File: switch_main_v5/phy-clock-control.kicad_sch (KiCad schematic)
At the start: 36 parts, among them Q1101 DMN21D2UFB-7B, Q1102 DMN21D2UFB-7B, Q1103 DMN21D2UFB-7B, U1101 NX3L4051HRZ, U1102 LMK1C1104DQFR, U1103 LMK1C1104DQFR

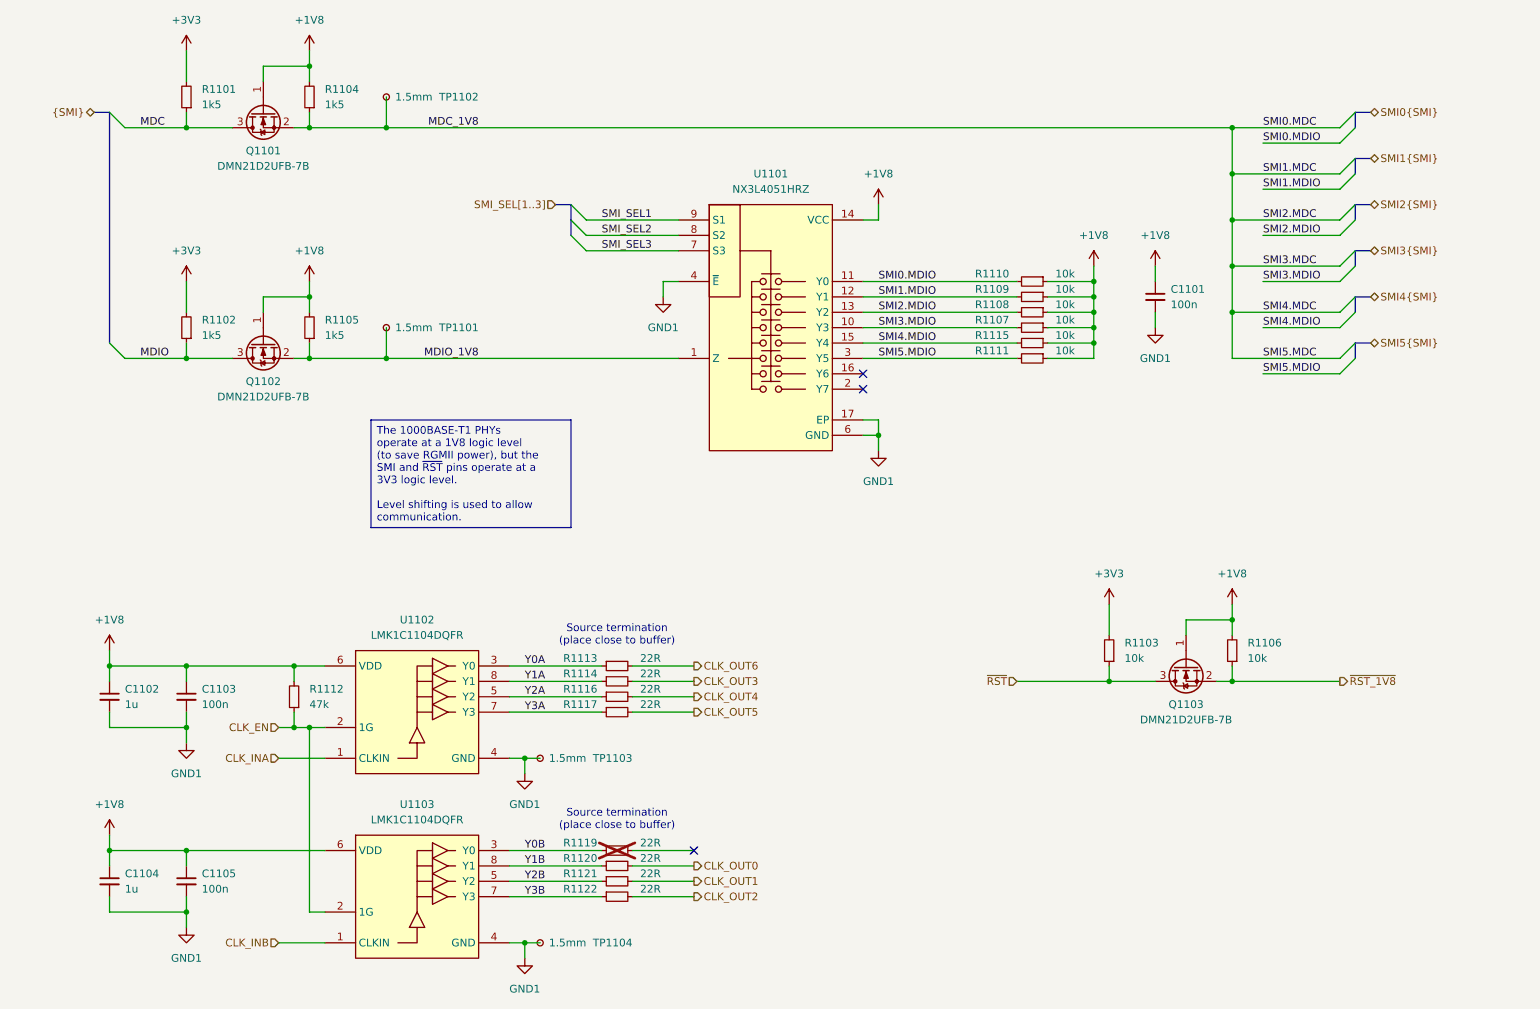
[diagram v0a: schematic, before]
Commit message: Updated 1v0_buck_converter feedback resistors
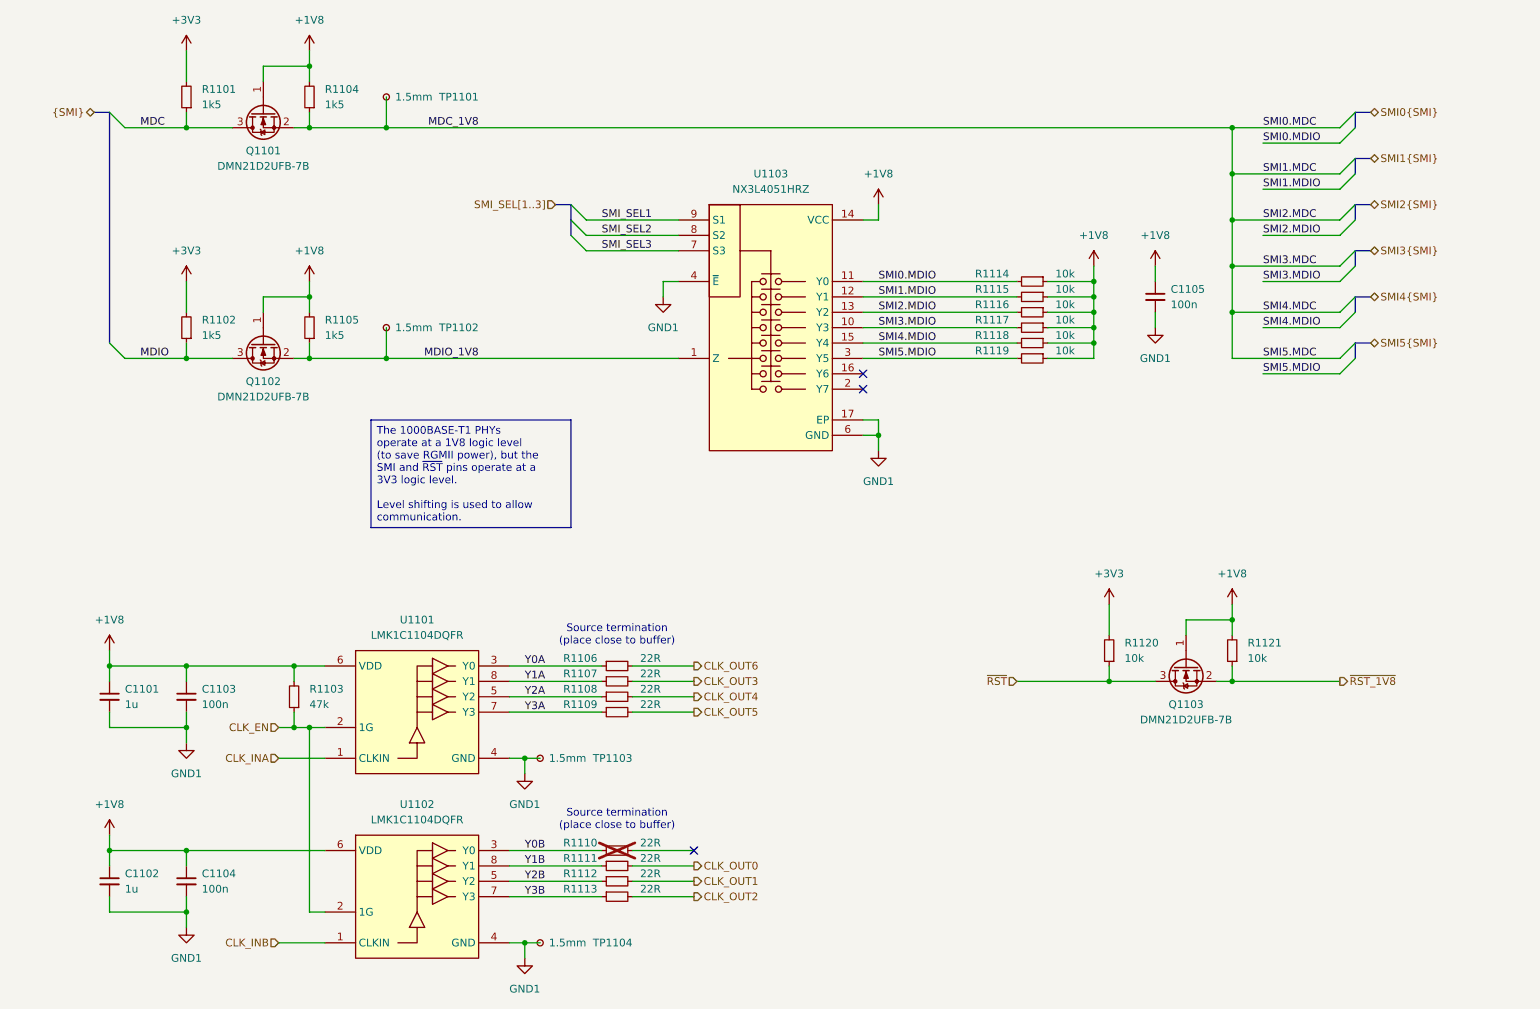
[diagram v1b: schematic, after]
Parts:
- renumbered C1102 to C1101, C1104 to C1102, C1105 to C1104, C1101 to C1105, R1112 to R1103, R1113 to R1106, R1114 to R1107, R1116 to R1108, R1117 to R1109, R1119 to R1110, R1120 to R1111, R1121 to R1112, R1122 to R1113, R1110 to R1114, R1109 to R1115, R1108 to R1116, R1107 to R1117, R1115 to R1118, R1111 to R1119, R1103 to R1120, R1106 to R1121, TP1102 to TP1101, TP1101 to TP1102, U1102 to U1101, U1103 to U1102, U1101 to U1103

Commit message: Changed main 3V3 regulator to 3A, added switch 2 crystal & other changes
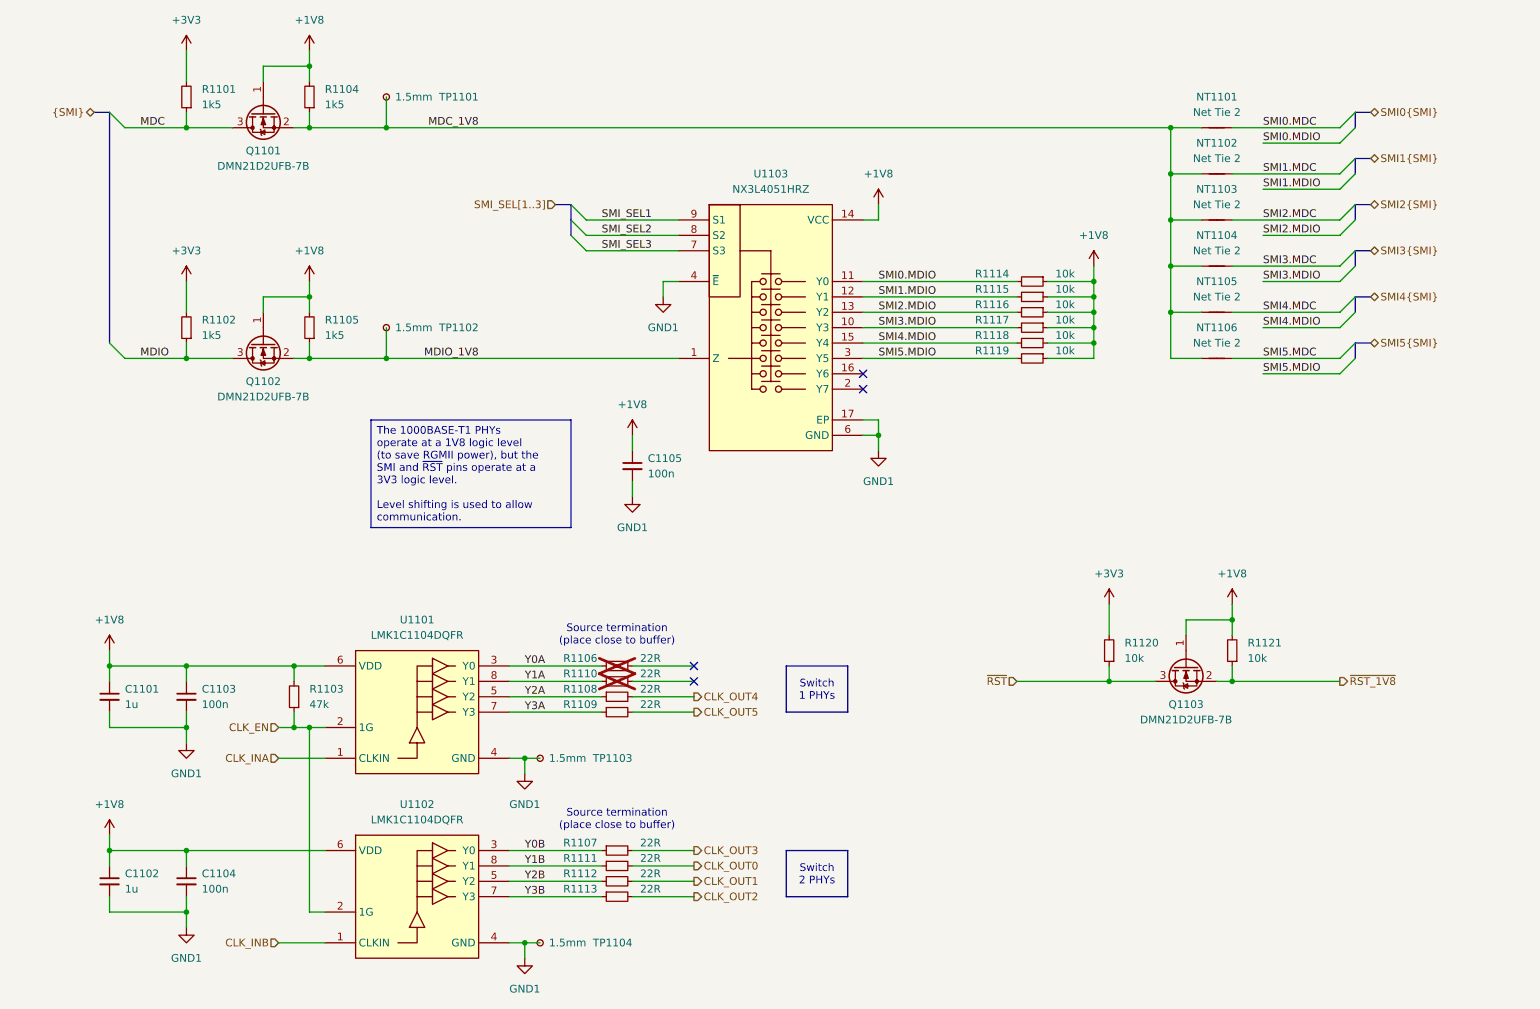
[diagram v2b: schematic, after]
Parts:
- added NT1101, NT1102, NT1103, NT1104, NT1105, NT1106: Net Tie 2, project_footprints:NetTie-2_SMD_Pad0.15mm, symbol NET-TIE:NetTie_2
- R1106: now not fitted; now left out of the parts list
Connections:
- net MDC_1V8: now also NT1101.1, NT1102.1, NT1103.1, NT1104.1, NT1105.1, NT1106.1
- net Y0B: now also R1107.1; no longer R1110.1
- net Y1A: now also R1110.1; no longer R1107.1
- net CLK_OUT6: no longer names the net of R1106.2
- new net SMI0.MDC: NT1101.2
- new net SMI1.MDC: NT1102.2
- new net SMI2.MDC: NT1103.2
- new net SMI3.MDC: NT1104.2
- new net SMI4.MDC: NT1105.2
- new net SMI5.MDC: NT1106.2
- no-connect marks 3 -> 4
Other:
- moved on the sheet: C1105, R1107, R1110

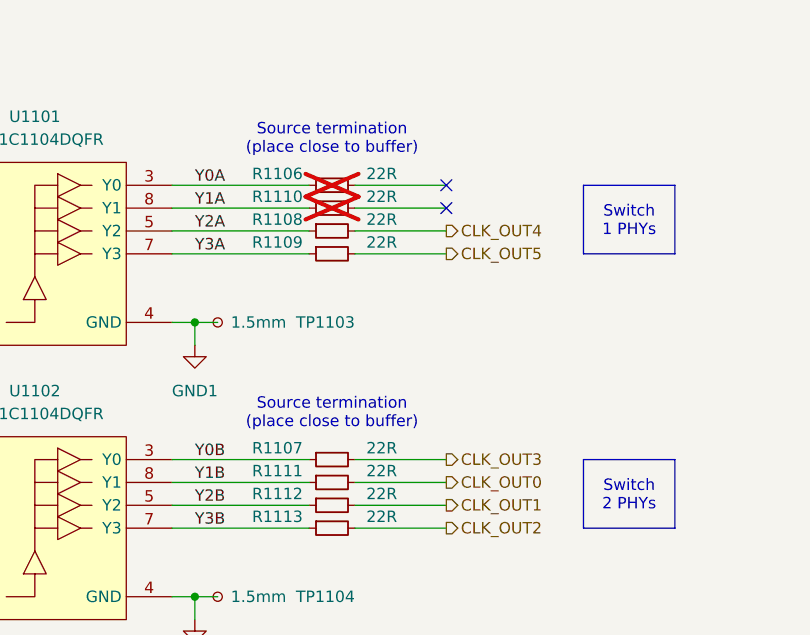
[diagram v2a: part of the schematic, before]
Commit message: Routed switch 1 clocking
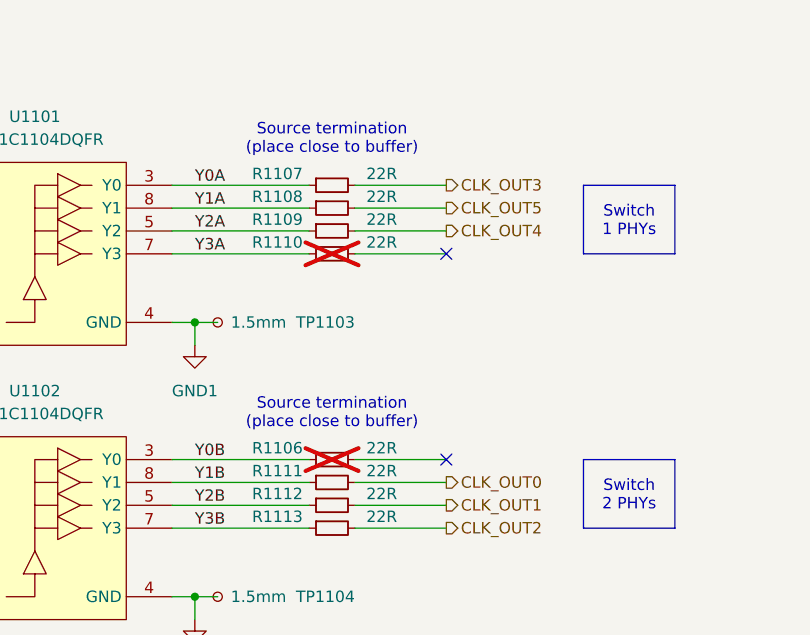
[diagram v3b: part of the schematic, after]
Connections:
- net CLK_OUT4: now also R1109.2; no longer R1108.2
- net CLK_OUT5: now also R1108.2; no longer R1109.2
- net Y0A: now also R1107.1; no longer R1106.1
- net Y0B: now also R1106.1; no longer R1107.1
- net Y1A: now also R1108.1; no longer R1110.1
- net Y2A: now also R1109.1; no longer R1108.1
- net Y3A: now also R1110.1; no longer R1109.1
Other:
- moved on the sheet: R1106, R1107, R1108, R1109, R1110
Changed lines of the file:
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@@
 	)
 	(no_connect
-		(at 139.7 132.08)
+		(at 139.7 137.16)
 	)
 	(no_connect
@@
 	)
 	(no_connect
-		(at 139.7 129.54)
+		(at 139.7 160.02)
 	)
 	(no_connect
@@
 	(hierarchical_label "CLK_OUT3"
 		(shape output)
-		(at 139.7 160.02 0)
+		(at 139.7 129.54 0)
 		(effects
 			(font
@@
 	(hierarchical_label "CLK_OUT5"
 		(shape output)
-		(at 139.7 137.16 0)
+		(at 139.7 132.08 0)
 		(effects
 			(font
@@
 	(symbol
 		(lib_id "Device:R_Small")
-		(at 127 160.02 90)
+		(at 127 129.54 90)
 		(mirror x)
 		(unit 1)
@@
 		(dnp no)
 		(property "Reference" "R1107"
-			(at 118.11 158.75 90)
+			(at 118.11 128.27 90)
 			(effects
 				(font
@@
 		)
 		(property "Value" "22R"
-			(at 130.81 158.75 90)
+			(at 130.81 128.27 90)
 			(effects
 				(font
@@
 		)
 		(property "Footprint" "Resistor_SMD:R_0402_1005Metric"
-			(at 127 160.02 0)
+			(at 127 129.54 0)
 			(effects
 				(font
@@
 		)
 		(property "Datasheet" "~"
-			(at 127 160.02 0)
+			(at 127 129.54 0)
 			(effects
 				(font
@@
 		)
 		(property "Description" "Resistor, small symbol"
-			(at 127 160.02 0)
+			(at 127 129.54 0)
 			(effects
 				(font
@@
 	(symbol
 		(lib_id "Device:R_Small")
-		(at 127 132.08 90)
+		(at 127 137.16 90)
 		(mirror x)
 		(unit 1)
@@
 		(dnp yes)
 		(property "Reference" "R1110"
-			(at 118.11 130.81 90)
+			(at 118.11 135.89 90)
 			(effects
 				(font
@@
 		)
 		(property "Value" "22R"
-			(at 130.81 130.81 90)
+			(at 130.81 135.89 90)
 			(effects
 				(font
@@
 		)
 		(property "Footprint" "Resistor_SMD:R_0402_1005Metric"
-			(at 127 132.08 0)
+			(at 127 137.16 0)
 			(effects
 				(font
@@
 		)
 		(property "Datasheet" "~"
-			(at 127 132.08 0)
+			(at 127 137.16 0)
 			(effects
 				(font
@@
 		)
 		(property "Description" "Resistor, small symbol"
-			(at 127 132.08 0)
+			(at 127 137.16 0)
 			(effects
 				(font
@@
 	(symbol
 		(lib_id "Device:R_Small")
-		(at 127 129.54 90)
+		(at 127 160.02 90)
 		(mirror x)
 		(unit 1)
@@
 		(dnp yes)
 		(property "Reference" "R1106"
-			(at 118.11 128.27 90)
+			(at 118.11 158.75 90)
 			(effects
 				(font
@@
 		)
 		(property "Value" "22R"
-			(at 130.81 128.27 90)
+			(at 130.81 158.75 90)
 			(effects
 				(font
@@
 		)
 		(property "Footprint" "Resistor_SMD:R_0402_1005Metric"
-			(at 127 129.54 0)
+			(at 127 160.02 0)
 			(effects
 				(font
@@
 		)
 		(property "Datasheet" "~"
-			(at 127 129.54 0)
+			(at 127 160.02 0)
 			(effects
 				(font
@@
 		)
 		(property "Description" "Resistor, small symbol"
-			(at 127 129.54 0)
+			(at 127 160.02 0)
 			(effects
 				(font
@@
 	(symbol
 		(lib_id "Device:R_Small")
-		(at 127 137.16 90)
+		(at 127 134.62 90)
 		(mirror x)
 		(unit 1)
@@
 		(dnp no)
 		(property "Reference" "R1109"
-			(at 118.11 135.89 90)
+			(at 118.11 133.35 90)
 			(effects
 				(font
@@
 		)
 		(property "Value" "22R"
-			(at 130.81 135.89 90)
+			(at 130.81 133.35 90)
 			(effects
 				(font
@@
 		)
 		(property "Footprint" "Resistor_SMD:R_0402_1005Metric"
-			(at 127 137.16 0)
+			(at 127 134.62 0)
 			(effects
 				(font
@@
 		)
 		(property "Datasheet" "~"
-			(at 127 137.16 0)
+			(at 127 134.62 0)
 			(effects
 				(font
@@
 		)
 		(property "Description" "Resistor, small symbol"
-			(at 127 137.16 0)
+			(at 127 134.62 0)
 			(effects
 				(font
@@
 	(symbol
 		(lib_id "Device:R_Small")
-		(at 127 134.62 90)
+		(at 127 132.08 90)
 		(mirror x)
 		(unit 1)
@@
 		(dnp no)
 		(property "Reference" "R1108"
-			(at 118.11 133.35 90)
+			(at 118.11 130.81 90)
 			(effects
 				(font
@@
 		)
 		(property "Value" "22R"
-			(at 130.81 133.35 90)
+			(at 130.81 130.81 90)
 			(effects
 				(font
@@
 		)
 		(property "Footprint" "Resistor_SMD:R_0402_1005Metric"
-			(at 127 134.62 0)
+			(at 127 132.08 0)
 			(effects
 				(font
@@
 		)
 		(property "Datasheet" "~"
-			(at 127 134.62 0)
+			(at 127 132.08 0)
 			(effects
 				(font
@@
 		)
 		(property "Description" "Resistor, small symbol"
-			(at 127 134.62 0)
+			(at 127 132.08 0)
 			(effects
 				(font

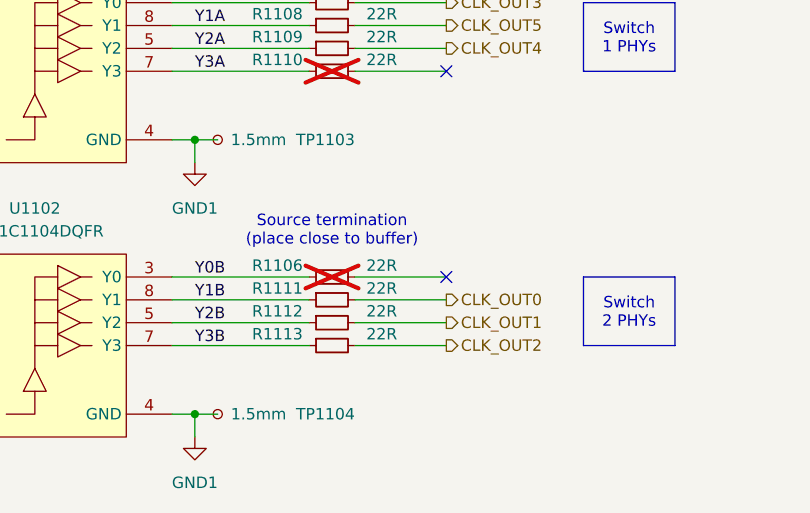
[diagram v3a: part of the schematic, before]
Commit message: PHY 1 & 2 routing progress and passive placement
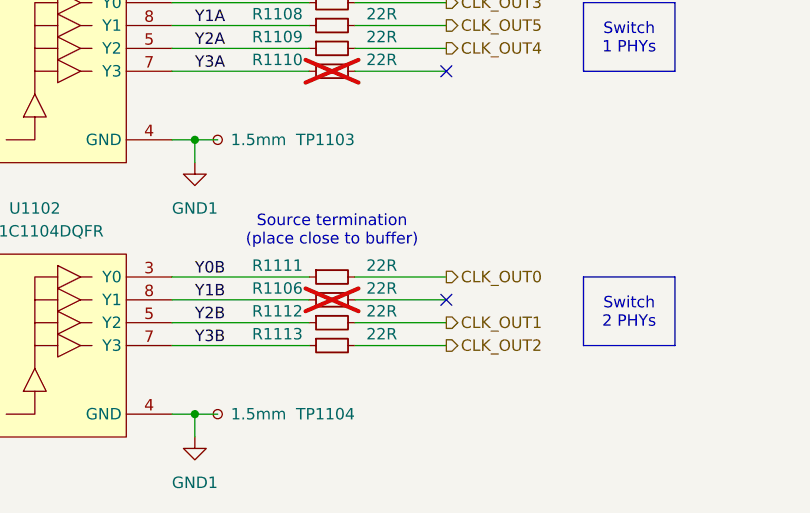
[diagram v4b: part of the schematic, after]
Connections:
- net Y0B: now also R1111.1; no longer R1106.1
- net Y1B: now also R1106.1; no longer R1111.1
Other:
- moved on the sheet: R1106, R1111
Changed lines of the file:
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@@
 	)
 	(no_connect
-		(at 139.7 160.02)
+		(at 139.7 162.56)
 	)
 	(no_connect
@@
 	(hierarchical_label "CLK_OUT0"
 		(shape output)
-		(at 139.7 162.56 0)
+		(at 139.7 160.02 0)
 		(effects
 			(font
@@
 	(symbol
 		(lib_id "Device:R_Small")
-		(at 127 160.02 90)
+		(at 127 162.56 90)
 		(mirror x)
 		(unit 1)
@@
 		(dnp yes)
 		(property "Reference" "R1106"
-			(at 118.11 158.75 90)
+			(at 118.11 161.29 90)
 			(effects
 				(font
@@
 		)
 		(property "Value" "22R"
-			(at 130.81 158.75 90)
+			(at 130.81 161.29 90)
 			(effects
 				(font
@@
 		)
 		(property "Footprint" "Resistor_SMD:R_0402_1005Metric"
-			(at 127 160.02 0)
+			(at 127 162.56 0)
 			(effects
 				(font
@@
 		)
 		(property "Datasheet" "~"
-			(at 127 160.02 0)
+			(at 127 162.56 0)
 			(effects
 				(font
@@
 		)
 		(property "Description" "Resistor, small symbol"
-			(at 127 160.02 0)
+			(at 127 162.56 0)
 			(effects
 				(font
@@
 	(symbol
 		(lib_id "Device:R_Small")
-		(at 127 162.56 90)
+		(at 127 160.02 90)
 		(mirror x)
 		(unit 1)
@@
 		(dnp no)
 		(property "Reference" "R1111"
-			(at 118.11 161.29 90)
+			(at 118.11 158.75 90)
 			(effects
 				(font
@@
 		)
 		(property "Value" "22R"
-			(at 130.81 161.29 90)
+			(at 130.81 158.75 90)
 			(effects
 				(font
@@
 		)
 		(property "Footprint" "Resistor_SMD:R_0402_1005Metric"
-			(at 127 162.56 0)
+			(at 127 160.02 0)
 			(effects
 				(font
@@
 		)
 		(property "Datasheet" "~"
-			(at 127 162.56 0)
+			(at 127 160.02 0)
 			(effects
 				(font
@@
 		)
 		(property "Description" "Resistor, small symbol"
-			(at 127 162.56 0)
+			(at 127 160.02 0)
 			(effects
 				(font
